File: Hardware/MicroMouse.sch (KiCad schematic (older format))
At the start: 45 parts

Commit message: Update design
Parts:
- added C10, C9: 1uF, symbol Device:C_Small
- added C13, C14: 0.1uF, symbol Device:C_Small
- added J4, J5: B5B-XH-A(LF)(SN), symbol Connector:Conn_01x05_Male
- added R11, R15, R16, R17, R20, R22: 10k, symbol Device:R_Small
- added R14, R19, R21: 150R, symbol Device:R_Small
- added R7, R8: 100k, symbol Device:R_Small
- added RV1, RV2, RV3: 10k, symbol Device:R_POT_TRIM
- added unit 4 of U2
- added U3: ULN2803ADW, symbol Mice_Sym:ULN2803ADW
- added U4: 74LVC1G332GV-Q100H, symbol Mice_Sym:74LVC1G332GV-Q100H
- added U5: ADCMP393ARZ, symbol Mice_Sym:ADCMP393ARZ
- added U6, U7, U8: TCRT1000, symbol Mice_Sym:TCRT1000
- gave numbers to parts that had none: 42
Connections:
- net labels added: FRT, LFT, RHT
- wire segments 152 -> 253
- no-connect marks 0 -> 1
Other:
- note added: "Left Motor"
- note added: "Right Motor"
- note added: "Sensor Feedback"
- note added: "Stepper Motor"
- moved on the sheet: U2A, U2B, U2C

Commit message: Create BOM
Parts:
- removed SW1, SW2, SW3, SW4, SW6, SW7: SPST, symbol Mice_Sym:SPST
- added D3: L196L-LIC-TR, symbol Device:LED_Small
- added J6: PPTC201LFBN-RC (05), symbol Connector:Conn_01x05_Female
- added R23: 150R, symbol Device:R_Small
- C15, C16: value 22pF -> 27pF
- C3: value 1700pF -> 1.5nF
- D2: value MMSZ5231B-7-F -> SZMMSZ9V1T1G
- J2: value 68024-102HLF -> PRPC040SFAN-RC (02)
- J3: value 78511-106HLF -> PRPC040SFAN-RC (06)
- R14, R19, R21: value 150R -> 220R
- R3: value 8.2k -> 9.1k
- R5: value 12k -> 11.8k
- R9: value 30.5k -> 30.1k
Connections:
- net +5V: now also R23.1
- net Aux: now also U2.4 (CVref/C2IN1+/Vref-/AN2/RA2), U3.2 (2B)
- net C1: now also J6.3 (Pin_3)
- net C2: now also J6.4 (Pin_4)
- net C3: now also J6.5 (Pin_5)
- net R1: no longer R7.1
- net R2: no longer R8.1
- net at U2.26 (~T1G~/AN13/RB5): now also D3.1 (K)
- new net: D3.2 (A), R23.2
- new net: J6.1 (Pin_1), R7.1
- new net: J6.2 (Pin_2), R8.1
- no-connect marks 1 -> 0
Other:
- moved on the sheet: R7, R8

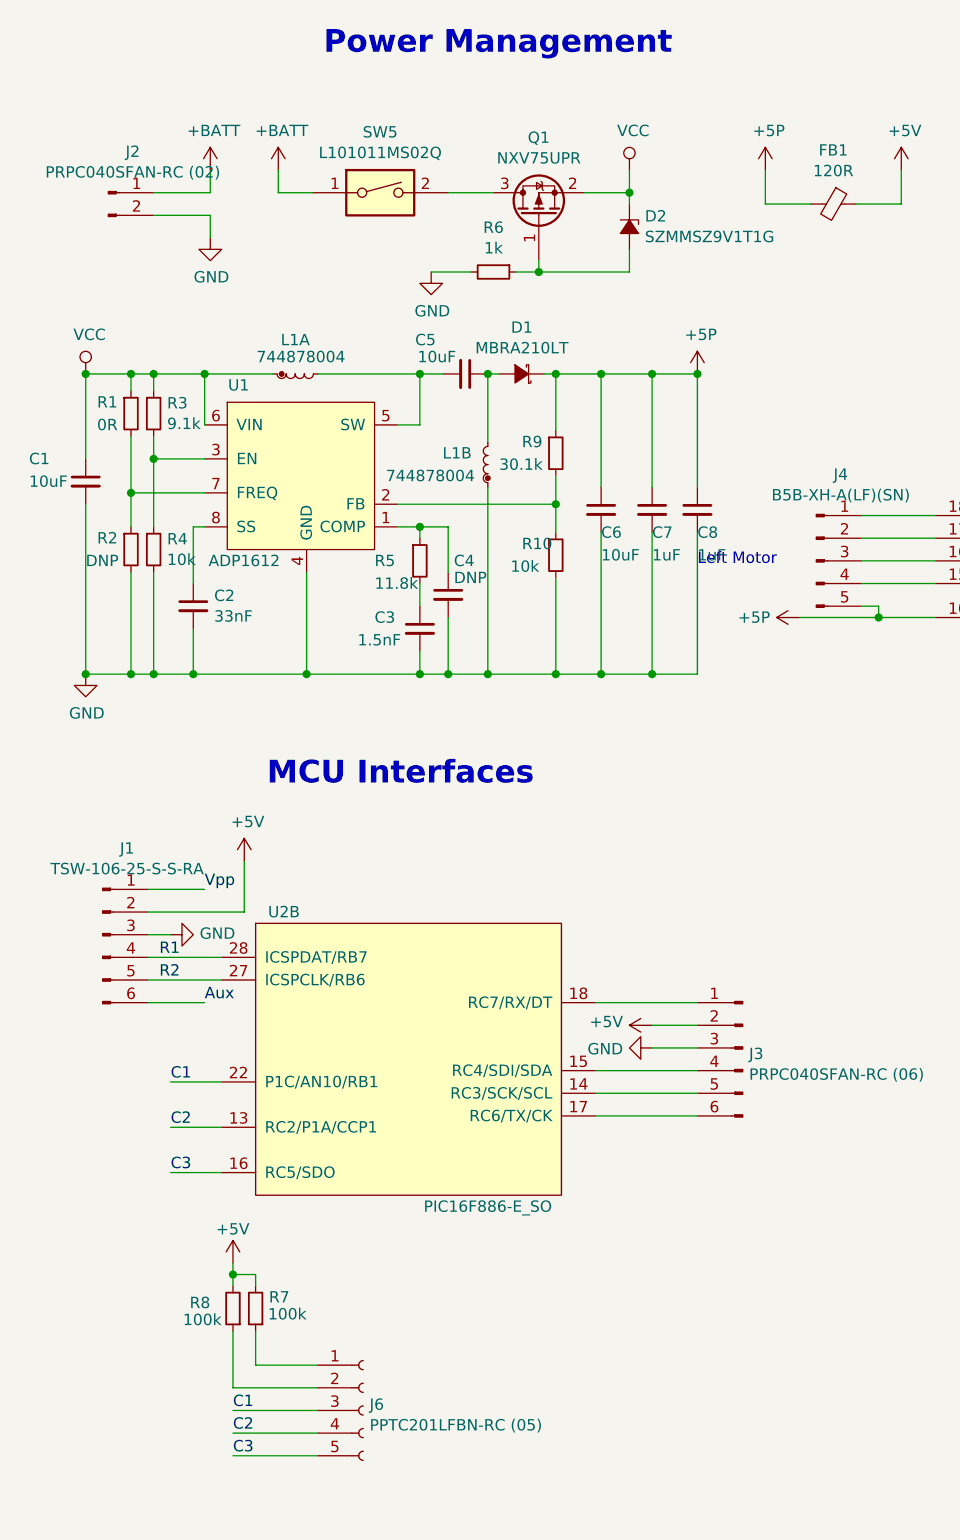
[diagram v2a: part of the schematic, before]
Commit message: Add battery holder and add matrix button
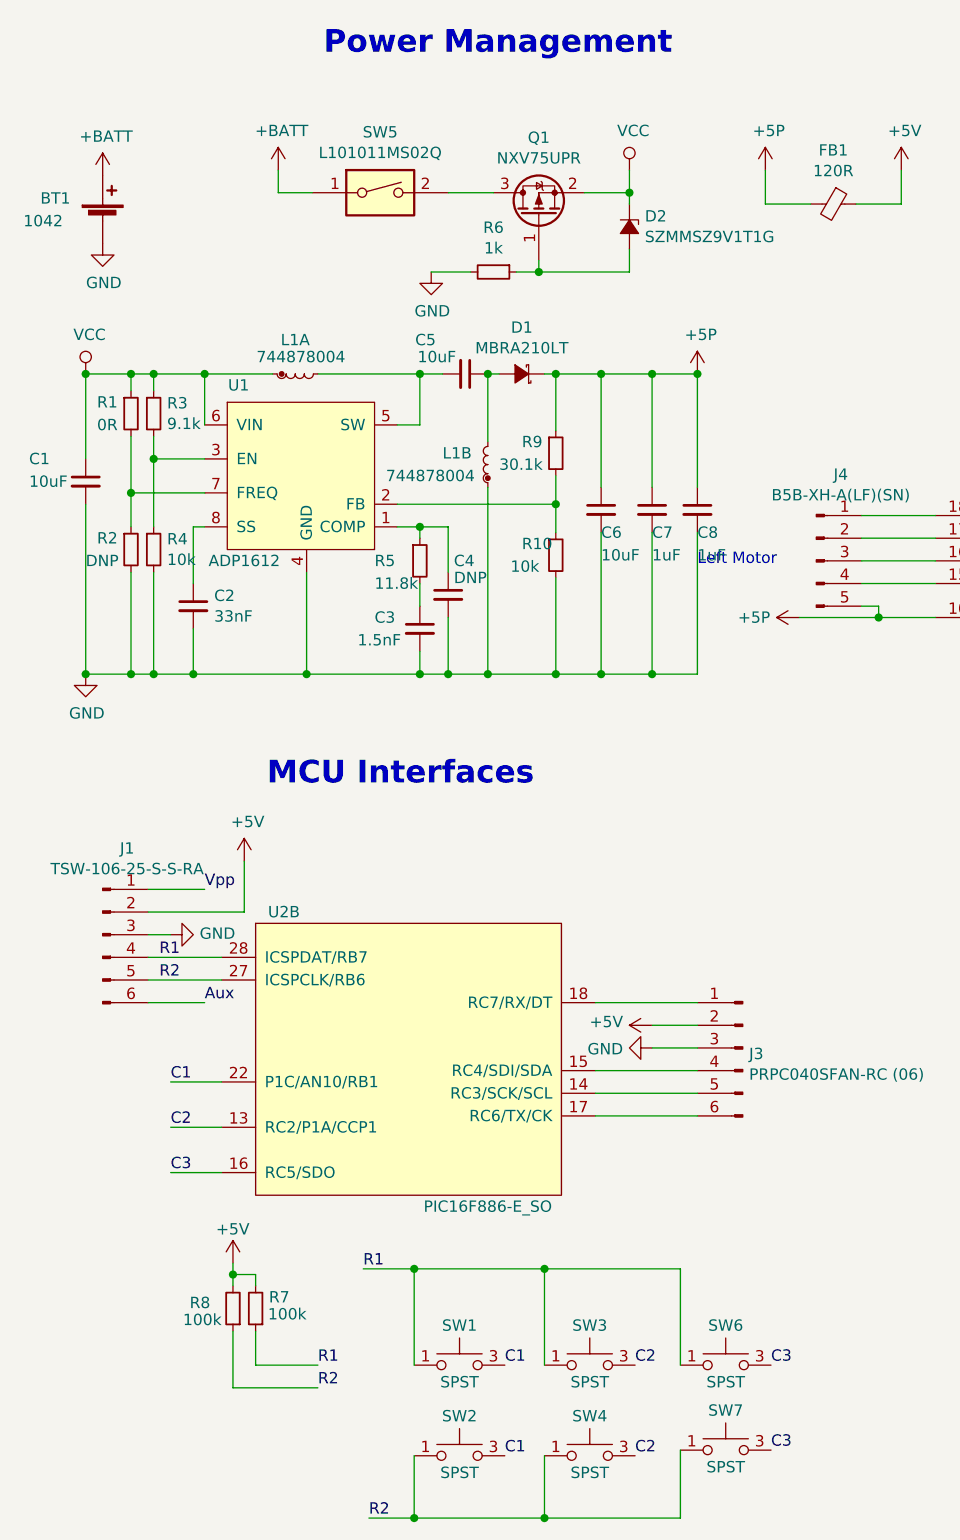
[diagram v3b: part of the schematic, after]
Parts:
- removed J2: PRPC040SFAN-RC (02), symbol Connector:Conn_01x02_Male
- removed J6: PPTC201LFBN-RC (05), symbol Connector:Conn_01x05_Female
- added BT1: 1042, symbol Device:Battery_Cell
- added SW1, SW2, SW3, SW4, SW6, SW7: SPST, symbol Mice_Sym:SPST
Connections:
- net +BATT: now also BT1.1 (+)
- net C1: now also SW1.3 (B), SW1.4 (B), SW2.3 (B), SW2.4 (B)
- net C2: now also SW3.3 (B), SW3.4 (B), SW4.3 (B), SW4.4 (B)
- net C3: now also SW6.3 (B), SW6.4 (B), SW7.3 (B), SW7.4 (B)
- net GND: now also BT1.2 (-)
- net R1: now also R7.1, SW1.1 (A), SW1.2 (A), SW3.1 (A), SW3.2 (A), SW6.1 (A), SW6.2 (A)
- net R2: now also R8.1, SW2.1 (A), SW2.2 (A), SW4.1 (A), SW4.2 (A), SW7.1 (A), SW7.2 (A)
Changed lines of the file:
@@
 Connection ~ 3400 1450
-$Comp
-L Connector:Conn_01x02_Male J2
-U 1 1 607144DA
-P 1100 1450
-F 0 "J2" H 1208 1631 50  0000 C CNN
-F 1 "PRPC040SFAN-RC (02)" H 1208 1540 50  0000 C CNN
-F 2 "" H 1100 1450 50  0001 C CNN
-F 3 "~" H 1100 1450 50  0001 C CNN
-	1    1100 1450
-	1    0    0    -1
-$EndComp
 $Comp
 L power:+BATT #PWR04
 U 1 1 6071C57A
-P 1550 1350
-F 0 "#PWR04" H 1550 1200 50  0001 C CNN
-F 1 "+BATT" H 1565 1523 50  0000 C CNN
-F 2 "" H 1550 1350 50  0001 C CNN
-F 3 "" H 1550 1350 50  0001 C CNN
-	1    1550 1350
+P 1075 1375
+F 0 "#PWR04" H 1075 1225 50  0001 C CNN
+F 1 "+BATT" H 1090 1548 50  0000 C CNN
+F 2 "" H 1075 1375 50  0001 C CNN
+F 3 "" H 1075 1375 50  0001 C CNN
+	1    1075 1375
 	1    0    0    -1
 $EndComp
@@
 L power:GND #PWR05
 U 1 1 6071C9C4
-P 1550 1650
-F 0 "#PWR05" H 1550 1400 50  0001 C CNN
-F 1 "GND" H 1555 1477 50  0000 C CNN
-F 2 "" H 1550 1650 50  0001 C CNN
-F 3 "" H 1550 1650 50  0001 C CNN
-	1    1550 1650
-	1    0    0    -1
-$EndComp
-Wire Wire Line
-	1300 1550 1550 1550
-Wire Wire Line
-	1550 1550 1550 1650
+P 1075 1675
+F 0 "#PWR05" H 1075 1425 50  0001 C CNN
+F 1 "GND" H 1080 1502 50  0000 C CNN
+F 2 "" H 1075 1675 50  0001 C CNN
+F 3 "" H 1075 1675 50  0001 C CNN
+	1    1075 1675
+	1    0    0    -1
+$EndComp
 $Comp
 L Device:Ferrite_Bead_Small FB1
@@
 Text Label 1375 5775 0    50   ~ 0
 C3
-Text Label 1650 6825 0    50   ~ 0
-C1
-Text Label 1650 6925 0    50   ~ 0
-C2
-Text Label 1650 7025 0    50   ~ 0
-C3
 $Comp
 L power:+5V #PWR012
@@
 Wire Wire Line
 	1275 4825 1600 4825
-$Comp
-L Connector:Conn_01x05_Female J6
-U 1 1 608570B2
-P 2225 6825
-F 0 "J6" H 2253 6851 50  0000 L CNN
-F 1 "PPTC201LFBN-RC (05)" H 2253 6760 50  0000 L CNN
-F 2 "" H 2225 6825 50  0001 C CNN
-F 3 "~" H 2225 6825 50  0001 C CNN
-	1    2225 6825
-	1    0    0    -1
-$EndComp
 Wire Wire Line
 	2025 6625 1750 6625
@@
 	1650 6725 1650 6475
 Wire Wire Line
-	2025 6825 1650 6825
-Wire Wire Line
-	2025 6925 1650 6925
-Wire Wire Line
-	2025 7025 1650 7025
-Wire Wire Line
 	1850 1350 1850 1450
 Wire Wire Line
 	1850 1450 2000 1450
-Wire Wire Line
-	1300 1450 1550 1450
-Wire Wire Line
-	1550 1450 1550 1350
 Wire Wire Line
 	6450 5575 6450 5525
@@
 Text Label 5750 2975 0    50   ~ 0
 Aux
+$Comp
+L Device:Battery_Cell BT1
+U 1 1 6069596B
+P 1075 1575
+F 0 "BT1" H 800 1675 50  0000 L CNN
+F 1 "1042" H 725 1575 50  0000 L CNN
+F 2 "" V 1075 1635 50  0001 C CNN
+F 3 "~" V 1075 1635 50  0001 C CNN
+	1    1075 1575
+	1    0    0    -1
+$EndComp
+$Comp
+L Mice_Sym:SPST SW1
+U 1 1 607143A7
+P 2650 6625
+F 0 "SW1" H 2650 6800 50  0000 C CNN
+F 1 "SPST" H 2650 6550 50  0000 C CNN
+F 2 "" H 2650 6625 50  0001 C CNN
+F 3 "" H 2650 6625 50  0001 C CNN
+	1    2650 6625
+	1    0    0    -1
+$EndComp
+$Comp
+L Mice_Sym:SPST SW3
+U 1 1 60715814
+P 3225 6625
+F 0 "SW3" H 3225 6800 50  0000 C CNN
+F 1 "SPST" H 3225 6550 50  0000 C CNN
+F 2 "" H 3225 6625 50  0001 C CNN
+F 3 "" H 3225 6625 50  0001 C CNN
+	1    3225 6625
+	1    0    0    -1
+$EndComp
+$Comp
+L Mice_Sym:SPST SW6
+U 1 1 60716018
+P 3825 6625
+F 0 "SW6" H 3825 6800 50  0000 C CNN
+F 1 "SPST" H 3825 6550 50  0000 C CNN
+F 2 "" H 3825 6625 50  0001 C CNN
+F 3 "" H 3825 6625 50  0001 C CNN
+	1    3825 6625
+	1    0    0    -1
+$EndComp
+$Comp
+L Mice_Sym:SPST SW7
+U 1 1 607174F2
+P 3825 7000
+F 0 "SW7" H 3825 7175 50  0000 C CNN
+F 1 "SPST" H 3825 6925 50  0000 C CNN
+F 2 "" H 3825 7000 50  0001 C CNN
+F 3 "" H 3825 7000 50  0001 C CNN
+	1    3825 7000
+	1    0    0    -1
+$EndComp
+$Comp
+L Mice_Sym:SPST SW4
+U 1 1 6071801C
+P 3225 7025
+F 0 "SW4" H 3225 7200 50  0000 C CNN
+F 1 "SPST" H 3225 6950 50  0000 C CNN
+F 2 "" H 3225 7025 50  0001 C CNN
+F 3 "" H 3225 7025 50  0001 C CNN
+	1    3225 7025
+	1    0    0    -1
+$EndComp
+$Comp
+L Mice_Sym:SPST SW2
+U 1 1 60718DF0
+P 2650 7025
+F 0 "SW2" H 2650 7200 50  0000 C CNN
+F 1 "SPST" H 2650 6950 50  0000 C CNN
+F 2 "" H 2650 7025 50  0001 C CNN
+F 3 "" H 2650 7025 50  0001 C CNN
+	1    2650 7025
+	1    0    0    -1
+$EndComp
+Text Label 2025 6625 0    50   ~ 0
+R1
+Text Label 2025 6725 0    50   ~ 0
+R2
+Wire Wire Line
+	3625 6625 3625 6200
+Wire Wire Line
+	3625 6200 3025 6200
+Wire Wire Line
+	2450 6625 2450 6200
+Connection ~ 2450 6200
+Wire Wire Line
+	2450 6200 2225 6200
+Wire Wire Line
+	3025 6625 3025 6200
+Connection ~ 3025 6200
+Wire Wire Line
+	3025 6200 2450 6200
+Wire Wire Line
+	3625 7000 3625 7300
+Wire Wire Line
+	3625 7300 3025 7300
+Wire Wire Line
+	2450 7025 2450 7300
+Connection ~ 2450 7300
+Wire Wire Line
+	2450 7300 2250 7300
+Wire Wire Line
+	3025 7025 3025 7300
+Connection ~ 3025 7300
+Wire Wire Line
+	3025 7300 2450 7300
+Text Label 2225 6200 0    50   ~ 0
+R1
+Text Label 2250 7300 0    50   ~ 0
+R2
+Text Label 2850 6625 0    50   ~ 0
+C1
+Text Label 2850 7025 0    50   ~ 0
+C1
+Text Label 3425 6625 0    50   ~ 0
+C2
+Text Label 3425 7025 0    50   ~ 0
+C2
+Text Label 4025 6625 0    50   ~ 0
+C3
+Text Label 4025 7000 0    50   ~ 0
+C3
 $EndSCHEMATC

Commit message: Add footprint to project
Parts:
- BT1: footprint (none) -> Micro-Footprint:1042-SMD
- C1, C5, C6: footprint (none) -> Micro-Footprint:CAP0805
- C10, C11, C12, C13, C14, C15, C16, C2, C3, C4, C7, C8, C9: footprint (none) -> Micro-Footprint:CAP0603
- D1: footprint (none) -> Micro-Footprint:MBRA210-SMA
- D2: footprint (none) -> Micro-Footprint:SZMMSZ9-SOD123
- D3, U6, U7, U8: footprint (none) -> Micro-Footprint:LTST-C170-0805
- FB1: footprint (none) -> Micro-Footprint:FER0603
- J1: footprint (none) -> Micro-Footprint:THRU-254-RHT-6P
- J3: footprint (none) -> Micro-Footprint:THRU-254-STR-6P
- J4, J5: footprint (none) -> Micro-Footprint:THRU-250-STR-5P
- L1: footprint (none) -> Micro-Footprint:744878004-SMD
- Q1: footprint (none) -> Micro-Footprint:NXV75UPR-SOT233
- R1, R10, R11, R12, R13, R14, R15, R16, R17, R18, R19, R2, R20, R21, R22, R23, R3, R4, R5, R6, R7, R8, R9: footprint (none) -> Micro-Footprint:RES0603
- RV1, RV2, RV3: footprint (none) -> Micro-Footprint:3306K-THRU
- SW1, SW2, SW3, SW4, SW6, SW7, SW8: footprint (none) -> Micro-Footprint:PTS526-4SMD
- SW5: footprint (none) -> Micro-Footprint:L101011-THRU
- U1: footprint (none) -> Micro-Footprint:ADP1612-8MSOP
- U2: footprint (none) -> Micro-Footprint:PIC16F886-28SOIC
- U3: footprint (none) -> Micro-Footprint:ULN2803A-18SO
- U4: footprint (none) -> Micro-Footprint:74LVC1G332-6TSOP
- U5: footprint (none) -> Micro-Footprint:ADCMP393-14SOIC
- Y1: footprint (none) -> Micro-Footprint:ECX1210-2SMD
